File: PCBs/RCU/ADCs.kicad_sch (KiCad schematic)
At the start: 12 parts

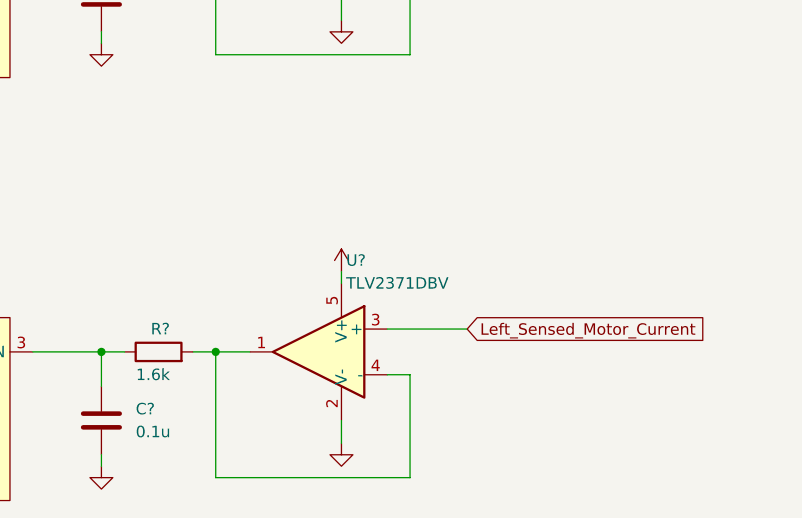
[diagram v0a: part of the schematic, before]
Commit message: Decreased paper size for motor control schematic and corrected the name of op amp used in ADC
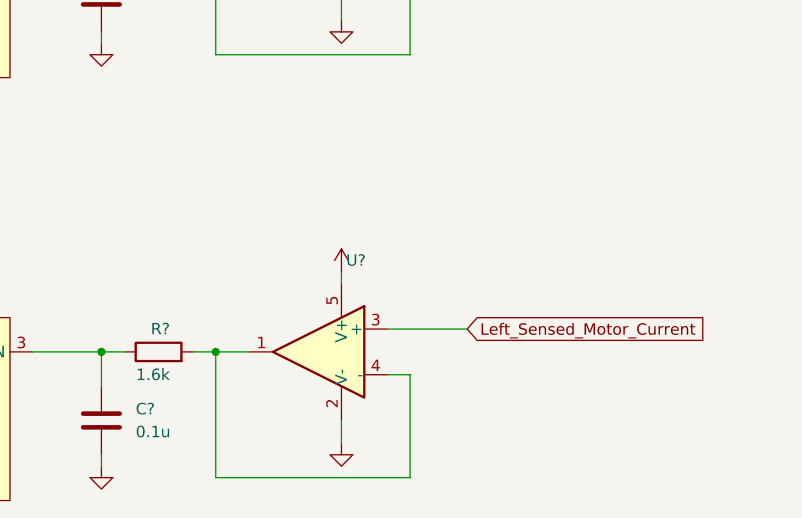
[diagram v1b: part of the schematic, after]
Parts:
- U?: value TLV2371DBV -> (none)
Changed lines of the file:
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@@
       (effects (font (size 1.27 1.27)) (justify right))
     )
-    (property "Value" "TLV2371DBV" (id 1) (at 124.9806 72.39 0)
+    (property "Value" "" (id 1) (at 124.9806 72.39 0)
       (effects (font (size 1.27 1.27)) (justify right))
     )

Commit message: Simulated how LPF and voltage buffer would affect current sensing reading
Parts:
- removed U?: (no value), Package_TO_SOT_SMD:SOT-23-5, symbol Amplifier_Operational:TLV2371DBV
- removed U?: (no value), symbol Amplifier_Operational:TLV2371DBV
- added U?: (no value), symbol Amplifier_Operational:OPA365xxD
- added U?: OPA365xxD, Package_SO:SOIC-8_3.9x4.9mm_P1.27mm, symbol Amplifier_Operational:OPA365xxD
- C?: value (none) -> 0.1u
- R?: value (none) -> 1.6k
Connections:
- net +3.3VA: now also U?.7 (V+), U?.7 (V+)
- net GND: now also U?.4 (V-), U?.4 (V-)
- net Left_Sensed_Motor_Current: now also U?.3 (+)
- net Right_Sensed_Motor_Current: now also U?.3 (+)
- net at R?.2: now also U?.2 (-), U?.6 (x2)
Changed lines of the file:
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@@
       (effects (font (size 1.27 1.27)) hide)
     )
-    (property "Value" "" (id 1) (at 124.46 67.31 0))
+    (property "Value" "+3.3VA" (id 1) (at 124.46 67.31 0))
     (property "Footprint" "" (id 2) (at 124.46 71.12 0)
       (effects (font (size 1.27 1.27)) hide)
@@
       (effects (font (size 1.27 1.27)) (justify left))
     )
-    (property "Value" "" (id 1) (at 105.41 35.56 90)
+    (property "Value" "1.6k" (id 1) (at 105.41 35.56 90)
       (effects (font (size 1.27 1.27)) (justify left))
     )
@@
     (pin "2")
   )
-  (symbol (lib_id "Amplifier_Operational:TLV2371DBV") (at 121.92 80.01 0) (mirror y) (unit 1)
-    (in_bom yes) (on_board yes) (fields_autoplaced)
-    (property "Reference" "U?" (id 0) (at 124.9806 69.85 0)
-      (effects (font (size 1.27 1.27)) (justify right))
-    )
-    (property "Value" "" (id 1) (at 124.9806 72.39 0)
-      (effects (font (size 1.27 1.27)) (justify right))
-    )
-    (property "Footprint" "Package_TO_SOT_SMD:SOT-23-5" (id 2) (at 124.46 85.09 0)
-      (effects (font (size 1.27 1.27)) (justify left) hide)
-    )
-    (property "Datasheet" "http://www.ti.com/lit/ds/symlink/tlv2375.pdf" (id 3) (at 121.92 74.93 0)
-      (effects (font (size 1.27 1.27)) hide)
-    )
-    (pin "2")
-    (pin "5")
-    (pin "1")
-    (pin "3")
-    (pin "4")
-  )
   (symbol (lib_id "power:GND") (at 48.26 88.9 0) (mirror y) (unit 1)
     (in_bom yes) (on_board yes) (fields_autoplaced)
@@
     )
     (pin "1")
-  )
-  (symbol (lib_id "Amplifier_Operational:TLV2371DBV") (at 121.92 33.02 0) (mirror y) (unit 1)
-    (in_bom yes) (on_board yes) (fields_autoplaced)
-    (property "Reference" "U?" (id 0) (at 124.9806 22.86 0)
-      (effects (font (size 1.27 1.27)) (justify right))
-    )
-    (property "Value" "" (id 1) (at 124.9806 25.4 0)
-      (effects (font (size 1.27 1.27)) (justify right))
-    )
-    (property "Footprint" "" (id 2) (at 124.46 38.1 0)
-      (effects (font (size 1.27 1.27)) (justify left) hide)
-    )
-    (property "Datasheet" "http://www.ti.com/lit/ds/symlink/tlv2375.pdf" (id 3) (at 121.92 27.94 0)
-      (effects (font (size 1.27 1.27)) hide)
-    )
-    (pin "2")
-    (pin "5")
-    (pin "1")
-    (pin "3")
-    (pin "4")
   )
   (symbol (lib_id "power:+3.3VA") (at 48.26 26.67 0) (unit 1)
@@
     (pin "5")
   )
+  (symbol (lib_id "Amplifier_Operational:OPA365xxD") (at 121.92 33.02 0) (mirror y) (unit 1)
+    (in_bom yes) (on_board yes) (fields_autoplaced)
+    (property "Reference" "U?" (id 0) (at 124.9806 22.86 0)
+      (effects (font (size 1.27 1.27)) (justify right))
+    )
+    (property "Value" "" (id 1) (at 124.9806 25.4 0)
+      (effects (font (size 1.27 1.27)) (justify right))
+    )
+    (property "Footprint" "" (id 2) (at 124.46 38.1 0)
+      (effects (font (size 1.27 1.27)) (justify left) hide)
+    )
+    (property "Datasheet" "http://www.ti.com/lit/ds/symlink/opa365.pdf" (id 3) (at 118.11 29.21 0)
+      (effects (font (size 1.27 1.27)) hide)
+    )
+    (pin "1")
+    (pin "2")
+    (pin "3")
+    (pin "4")
+    (pin "5")
+    (pin "6")
+    (pin "7")
+    (pin "8")
+  )
+  (symbol (lib_id "Amplifier_Operational:OPA365xxD") (at 121.92 80.01 0) (mirror y) (unit 1)
+    (in_bom yes) (on_board yes) (fields_autoplaced)
+    (property "Reference" "U?" (id 0) (at 124.9806 69.85 0)
+      (effects (font (size 1.27 1.27)) (justify right))
+    )
+    (property "Value" "OPA365xxD" (id 1) (at 124.9806 72.39 0)
+      (effects (font (size 1.27 1.27)) (justify right))
+    )
+    (property "Footprint" "Package_SO:SOIC-8_3.9x4.9mm_P1.27mm" (id 2) (at 124.46 85.09 0)
+      (effects (font (size 1.27 1.27)) (justify left) hide)
+    )
+    (property "Datasheet" "http://www.ti.com/lit/ds/symlink/opa365.pdf" (id 3) (at 118.11 76.2 0)
+      (effects (font (size 1.27 1.27)) hide)
+    )
+    (pin "1")
+    (pin "2")
+    (pin "3")
+    (pin "4")
+    (pin "5")
+    (pin "6")
+    (pin "7")
+    (pin "8")
+  )
   (symbol (lib_id "power:GND") (at 97.79 92.71 0) (unit 1)
     (in_bom yes) (on_board yes) (fields_autoplaced)
@@
       (effects (font (size 1.27 1.27)) (justify right))
     )
-    (property "Value" "" (id 1) (at 101.6 41.9099 0)
-      (effects (font (size 1.27 1.27)) (justify right))
-    )
+    (property "Value" "0.1u" (id 1) (at 101.6 41.9099 0)
+      (effects (font (size 1.27 1.27)) (justify right))
+    )

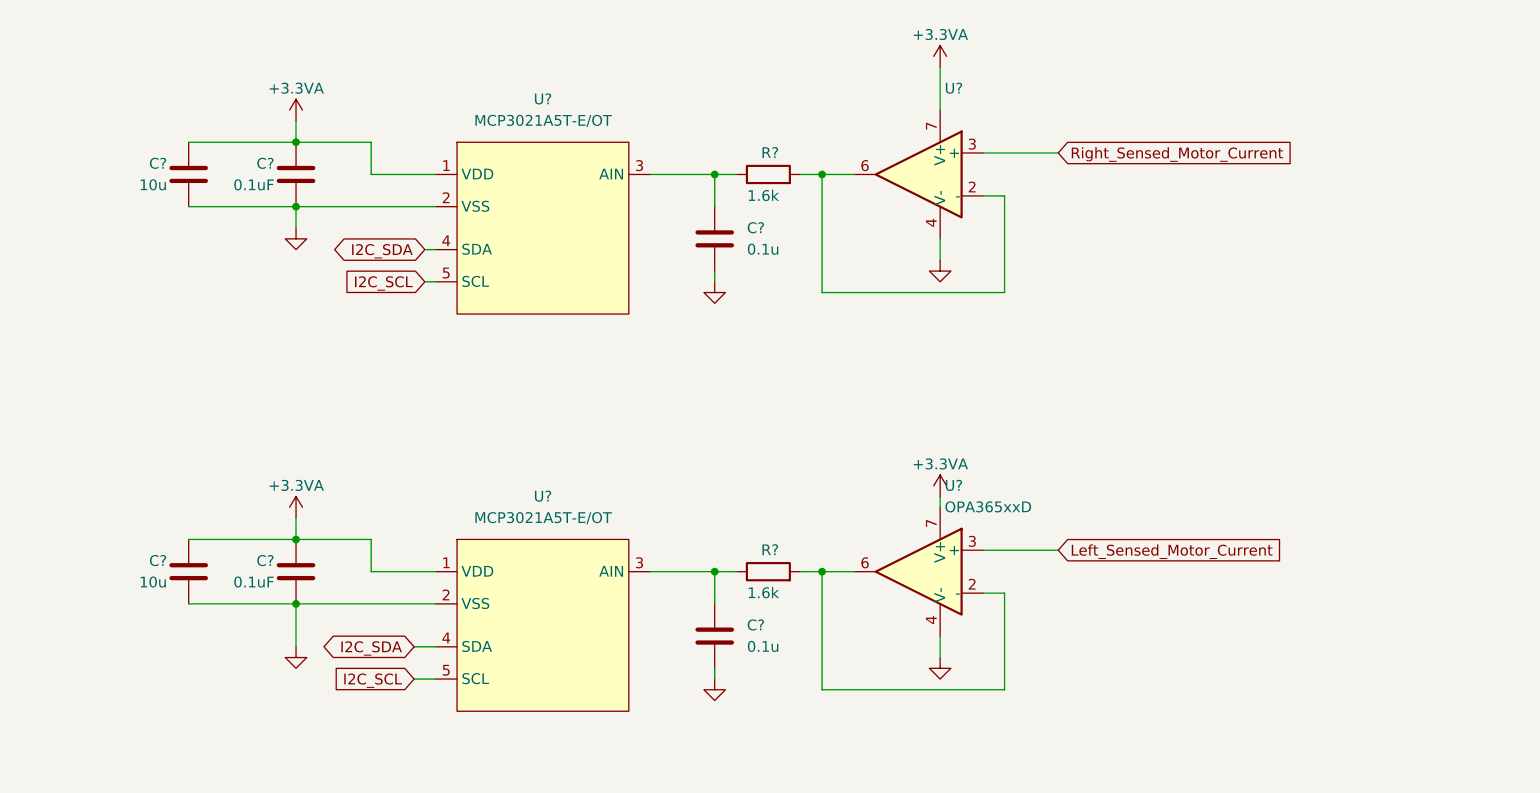
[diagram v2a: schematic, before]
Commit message: Add output buffer to IPROPI pin of Motor Driver ICs and low pass RC filter and input buffer to ADCs
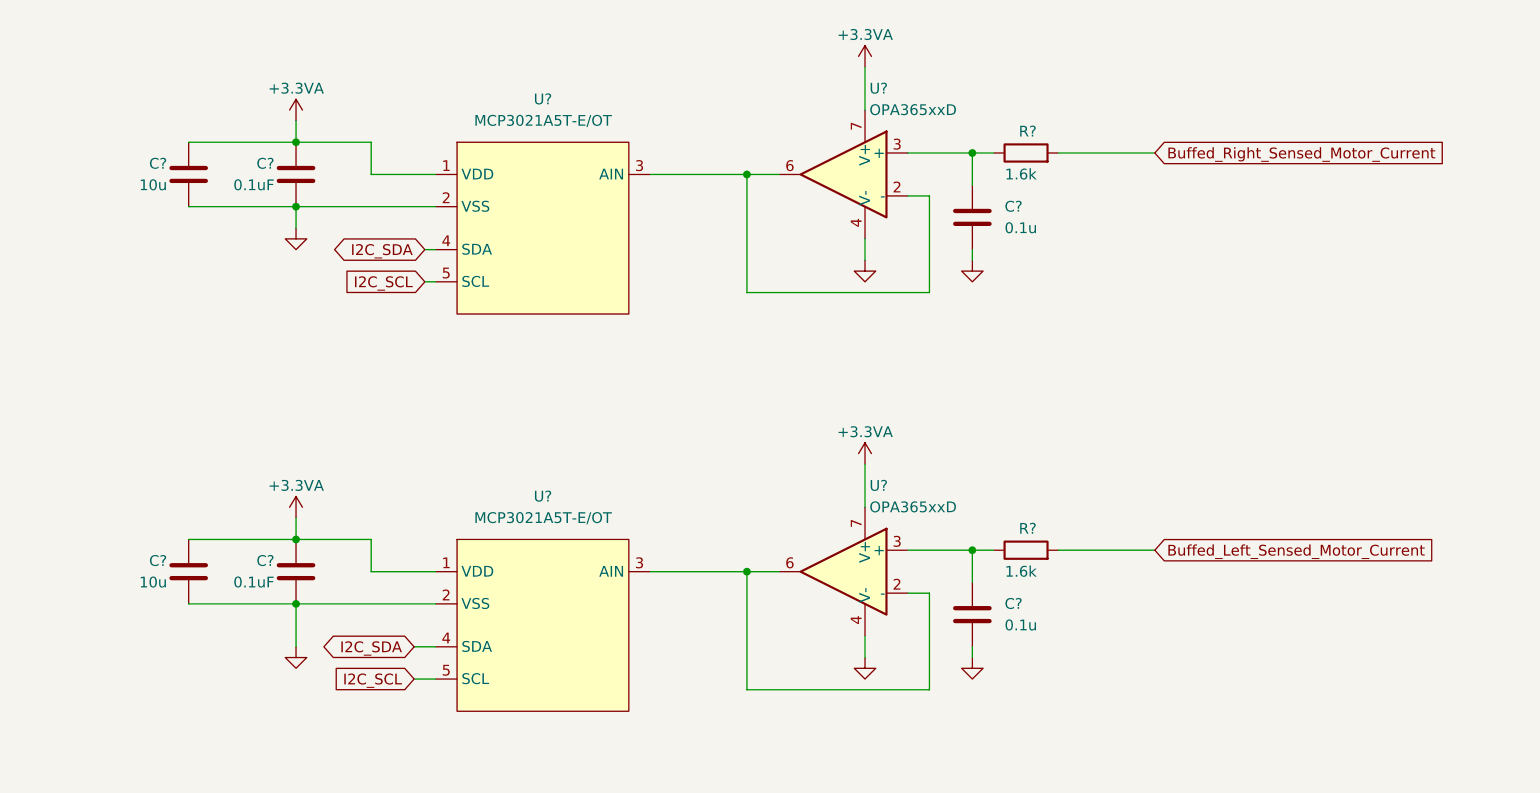
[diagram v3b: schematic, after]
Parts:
- removed C? (x2): 0.1u, symbol Device:C
- removed R? (x2): 1.6k, symbol Device:R
- added C? (x2): 0.1u, symbol Device:C
- added R? (x2): 1.6k, symbol Device:R
- U?: value (none) -> OPA365xxD; footprint (none) -> Package_SO:SOIC-8_3.9x4.9mm_P1.27mm
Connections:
- net GND: now also C?.1, C?.1
- net at U?.3 (AIN): now also U?.2 (-), U?.6 (x2)
- net Left_Sensed_Motor_Current: no longer names the net of U?.3 (+)
- net Left_Sensed_Motor_Current: now also C?.2, R?.1
- net Right_Sensed_Motor_Current: no longer names the net of U?.3 (+)
- net Right_Sensed_Motor_Current: now also C?.2, R?.1
- new net Buffed_Left_Sensed_Motor_Current: R?.2
- new net Buffed_Right_Sensed_Motor_Current: R?.2
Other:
- moved on the sheet: U?

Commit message: Numbered and ordered all of the modules
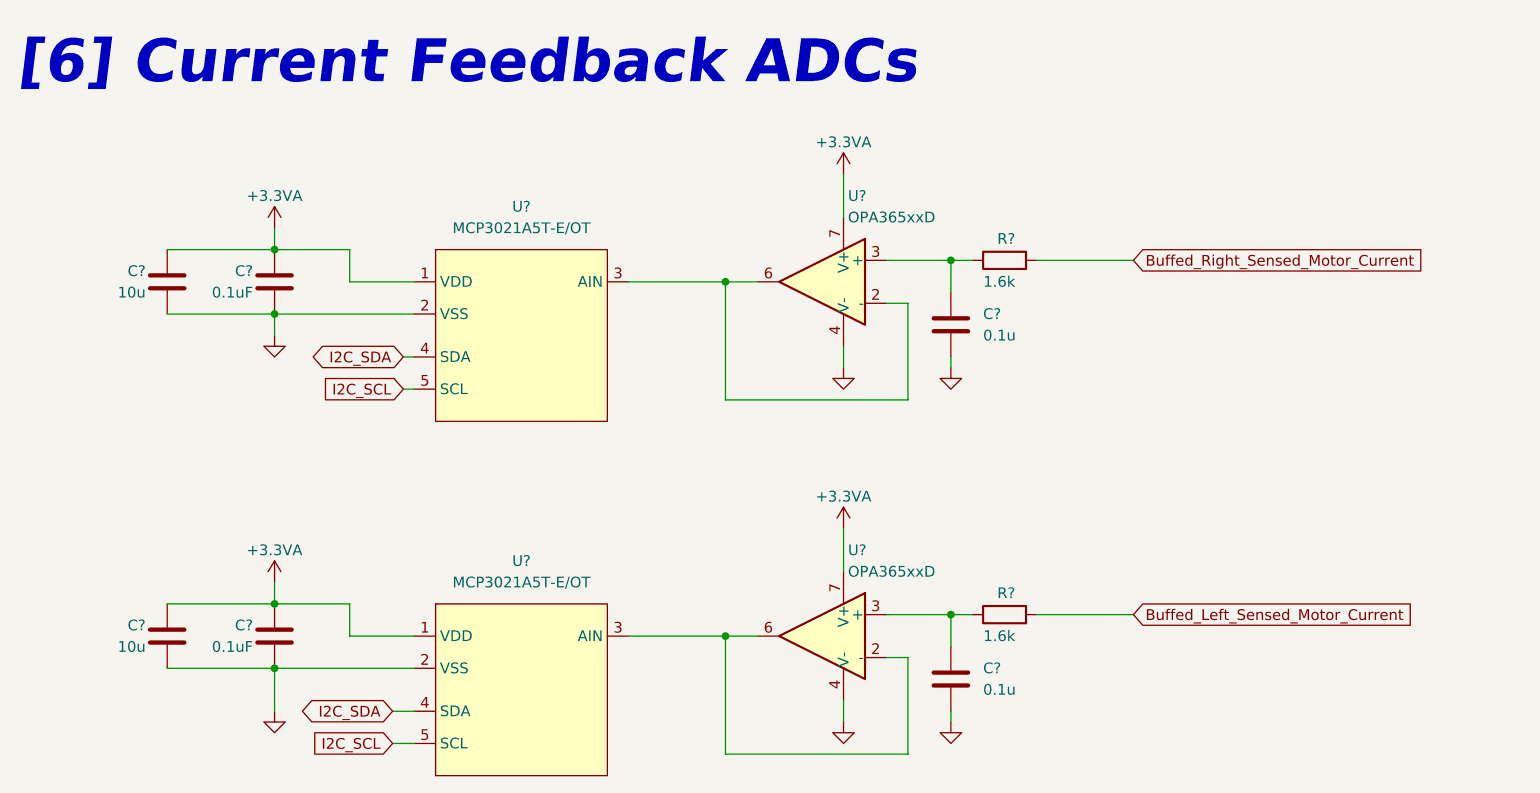
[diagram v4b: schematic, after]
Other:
- note added: "[6] Current Feedback ADCs"
- moved on the sheet: C?, R?, U?

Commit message: Annotated all components in ADC schematic
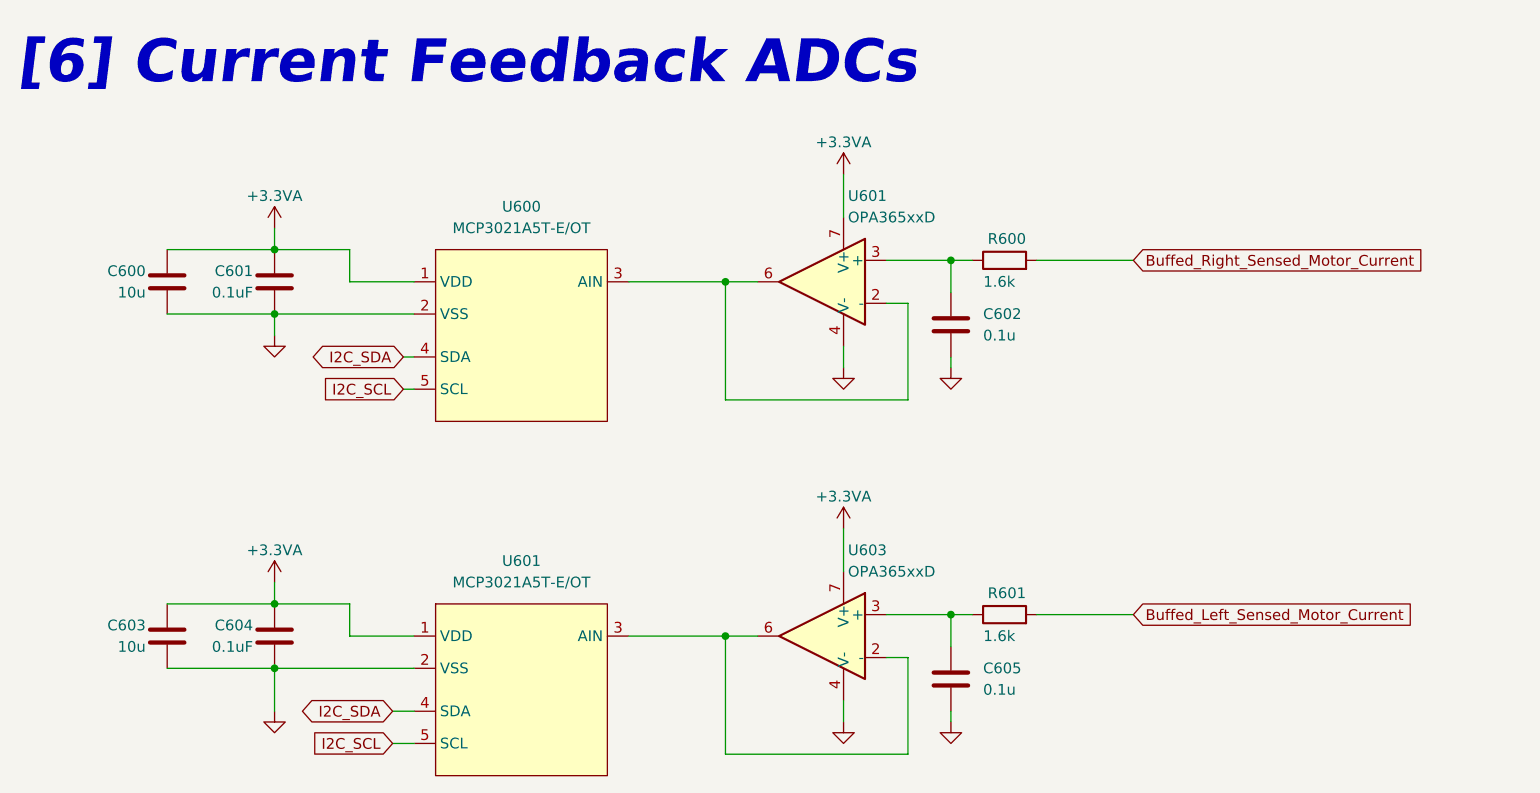
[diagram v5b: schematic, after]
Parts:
- gave numbers to parts that had none: 11
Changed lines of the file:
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@@
   (symbol (lib_id "Device:R") (at 132.08 43.18 90) (unit 1)
     (in_bom yes) (on_board yes)
-    (property "Reference" "R?" (id 0) (at 133.35 40.64 90)
+    (property "Reference" "R600" (id 0) (at 134.62 40.64 90)
       (effects (font (size 1.27 1.27)) (justify left))
     )
@@
   (symbol (lib_id "Device:C") (at 45.72 45.72 0) (mirror y) (unit 1)
     (in_bom yes) (on_board yes)
-    (property "Reference" "C?" (id 0) (at 43.18 44.45 0)
+    (property "Reference" "C601" (id 0) (at 43.18 44.45 0)
       (effects (font (size 1.27 1.27)) (justify left))
     )
@@
   (symbol (lib_id "Device:C") (at 125.73 92.71 180) (unit 1)
     (in_bom yes) (on_board yes) (fields_autoplaced)
-    (property "Reference" "C?" (id 0) (at 129.54 91.4399 0)
+    (property "Reference" "C605" (id 0) (at 129.54 91.4399 0)
       (effects (font (size 1.27 1.27)) (justify right))
     )
@@
   (symbol (lib_id "Device:C") (at 33.02 45.72 0) (mirror y) (unit 1)
     (in_bom yes) (on_board yes)
-    (property "Reference" "C?" (id 0) (at 30.48 44.45 0)
+    (property "Reference" "C600" (id 0) (at 30.48 44.45 0)
       (effects (font (size 1.27 1.27)) (justify left))
     )
@@
   (symbol (lib_id "Ghanis_Symbols_KiCad6:MCP3021A5T-E{slash}OT") (at 74.93 64.77 0) (unit 1)
     (in_bom yes) (on_board yes) (fields_autoplaced)
-    (property "Reference" "U?" (id 0) (at 74.93 36.83 0))
+    (property "Reference" "U600" (id 0) (at 74.93 36.83 0))
     (property "Value" "MCP3021A5T-E/OT" (id 1) (at 74.93 39.37 0))
     (property "Footprint" "" (id 2) (at 74.93 68.58 0)
@@
   (symbol (lib_id "Amplifier_Operational:OPA365xxD") (at 110.49 45.72 0) (mirror y) (unit 1)
     (in_bom yes) (on_board yes) (fields_autoplaced)
-    (property "Reference" "U?" (id 0) (at 113.5506 35.56 0)
+    (property "Reference" "U601" (id 0) (at 113.5506 35.56 0)
       (effects (font (size 1.27 1.27)) (justify right))
     )
@@
   (symbol (lib_id "Amplifier_Operational:OPA365xxD") (at 110.49 87.63 0) (mirror y) (unit 1)
     (in_bom yes) (on_board yes) (fields_autoplaced)
-    (property "Reference" "U?" (id 0) (at 113.5506 77.47 0)
+    (property "Reference" "U603" (id 0) (at 113.5506 77.47 0)
       (effects (font (size 1.27 1.27)) (justify right))
     )
@@
   (symbol (lib_id "Device:C") (at 33.02 87.63 0) (mirror y) (unit 1)
     (in_bom yes) (on_board yes)
-    (property "Reference" "C?" (id 0) (at 30.48 86.36 0)
+    (property "Reference" "C603" (id 0) (at 30.48 86.36 0)
       (effects (font (size 1.27 1.27)) (justify left))
     )
@@
   (symbol (lib_id "Device:C") (at 45.72 87.63 0) (mirror y) (unit 1)
     (in_bom yes) (on_board yes)
-    (property "Reference" "C?" (id 0) (at 43.18 86.36 0)
+    (property "Reference" "C604" (id 0) (at 43.18 86.36 0)
       (effects (font (size 1.27 1.27)) (justify left))
     )
@@
   (symbol (lib_id "Device:R") (at 132.08 85.09 90) (unit 1)
     (in_bom yes) (on_board yes)
-    (property "Reference" "R?" (id 0) (at 133.35 82.55 90)
+    (property "Reference" "R601" (id 0) (at 134.62 82.55 90)
       (effects (font (size 1.27 1.27)) (justify left))
     )
@@
   (symbol (lib_id "Device:C") (at 125.73 50.8 180) (unit 1)
     (in_bom yes) (on_board yes) (fields_autoplaced)
-    (property "Reference" "C?" (id 0) (at 129.54 49.5299 0)
+    (property "Reference" "C602" (id 0) (at 129.54 49.5299 0)
       (effects (font (size 1.27 1.27)) (justify right))
     )
@@
   (symbol (lib_id "Ghanis_Symbols_KiCad6:MCP3021A5T-E{slash}OT") (at 74.93 106.68 0) (unit 1)
     (in_bom yes) (on_board yes) (fields_autoplaced)
-    (property "Reference" "U?" (id 0) (at 74.93 78.74 0))
+    (property "Reference" "U601" (id 0) (at 74.93 78.74 0))
     (property "Value" "MCP3021A5T-E/OT" (id 1) (at 74.93 81.28 0))
     (property "Footprint" "" (id 2) (at 74.93 110.49 0)
